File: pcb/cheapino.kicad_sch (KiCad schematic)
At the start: 3 parts

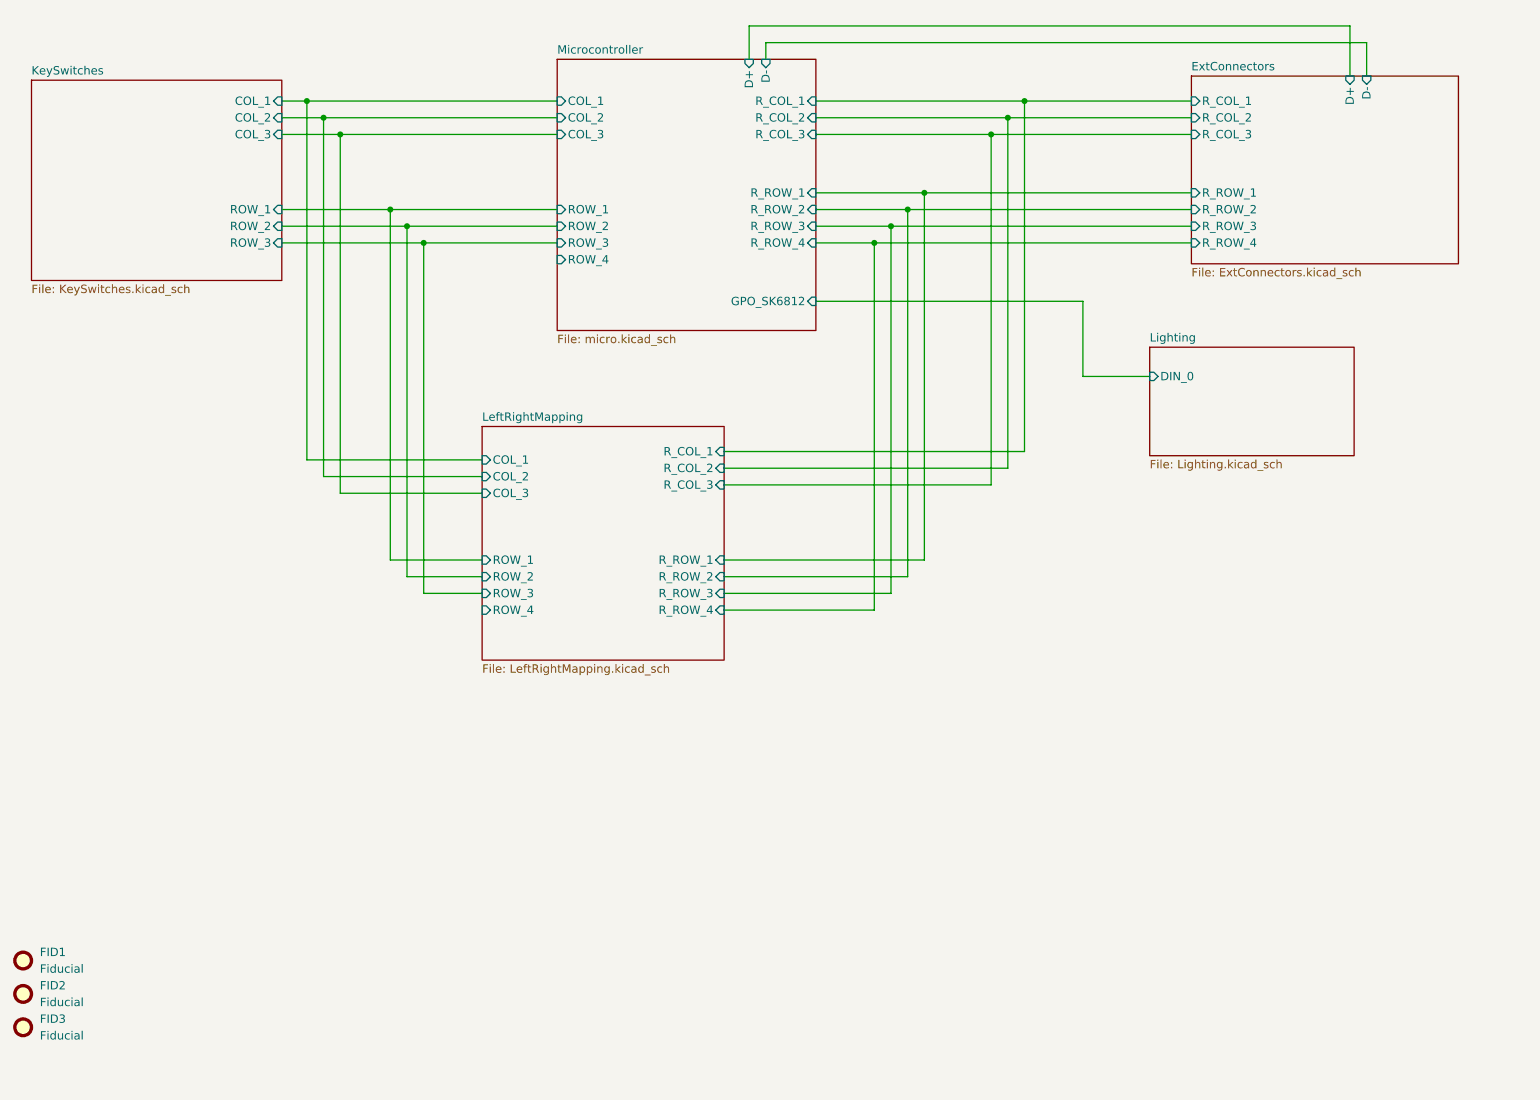
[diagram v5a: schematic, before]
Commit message: Placing more components onto the PCB and removing more stale leftovers from the now absent Rotary Encoder.
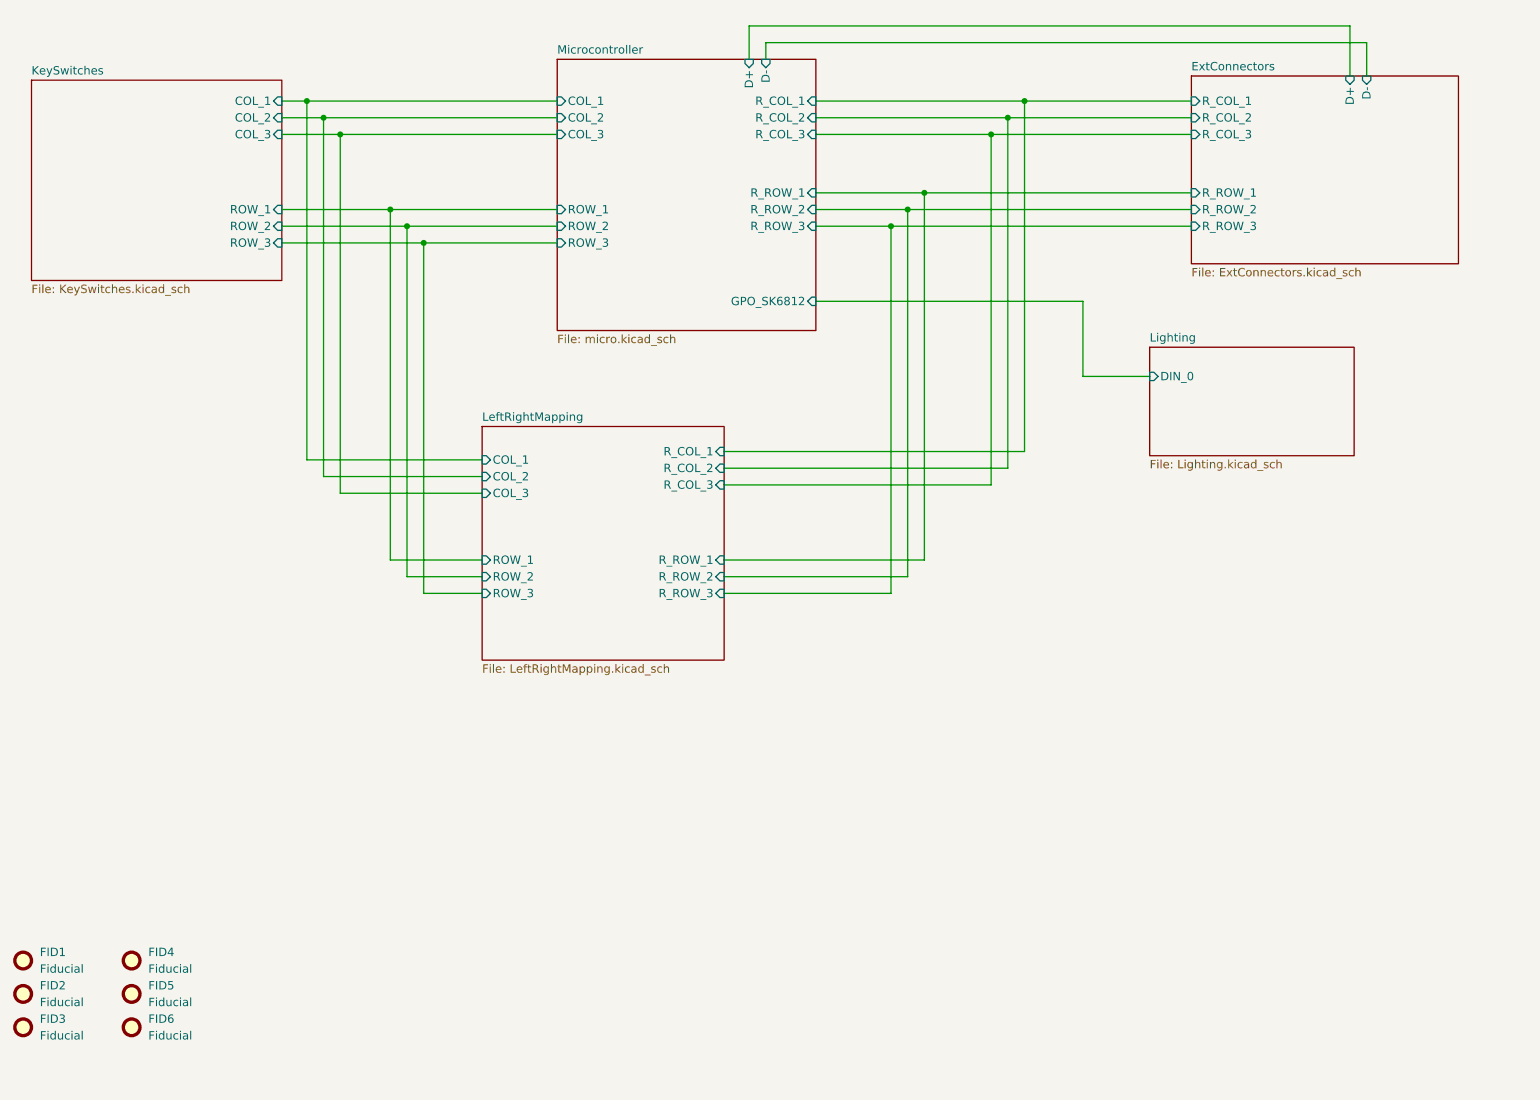
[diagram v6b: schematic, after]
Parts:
- added FID4, FID5, FID6: Fiducial, Fiducial:Fiducial_1mm_Mask2mm, symbol Mechanical:Fiducial
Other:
- sheet ExtConnectors ports: added none; removed R_ROW_4
- sheet LeftRightMapping ports: added none; removed ROW_4, R_ROW_4
- sheet Microcontroller ports: added none; removed ROW_4, R_ROW_4
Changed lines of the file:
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@@
-	)
-	(junction
-		(at 161.29 66.04)
-		(diameter 0)
-		(color 0 0 0 0)
 	)
 	(junction
@@
 	(wire
 		(pts
-			(xy 138.43 121.92) (xy 161.29 121.92)
-		)
-		(stroke
-			(width 0)
-			(type default)
-		)
-	)
-	(wire
-		(pts
 			(xy 166.37 116.84) (xy 138.43 116.84)
 		)
@@
 	(wire
 		(pts
-			(xy 161.29 66.04) (xy 161.29 121.92)
-		)
-		(stroke
-			(width 0)
-			(type default)
-		)
-	)
-	(wire
-		(pts
 			(xy 166.37 60.96) (xy 209.55 60.96)
 		)
@@
 	(wire
 		(pts
-			(xy 161.29 66.04) (xy 152.4 66.04)
-		)
-		(stroke
-			(width 0)
-			(type default)
-		)
-	)
-	(wire
-		(pts
-			(xy 209.55 66.04) (xy 161.29 66.04)
-		)
-		(stroke
-			(width 0)
-			(type default)
-		)
-	)
-	(wire
-		(pts
 			(xy 87.63 60.96) (xy 87.63 114.3)
 		)
@@
 			(width 0)
 			(type default)
+		)
+	)
+	(symbol
+		(lib_id "Mechanical:Fiducial")
+		(at 48.26 185.42 0)
+		(unit 1)
+		(exclude_from_sim yes)
+		(in_bom no)
+		(on_board yes)
+		(dnp no)
+		(fields_autoplaced yes)
+		(property "Reference" "FID6"
+			(at 50.8 184.1499 0)
+			(effects
+				(font
+					(size 1.27 1.27)
+				)
+				(justify left)
+			)
+		)
+		(property "Value" "Fiducial"
+			(at 50.8 186.6899 0)
+			(effects
+				(font
+					(size 1.27 1.27)
+				)
+				(justify left)
+			)
+		)
+		(property "Footprint" "Fiducial:Fiducial_1mm_Mask2mm"
+			(at 48.26 185.42 0)
+			(effects
+				(font
+					(size 1.27 1.27)
+				)
+				(hide yes)
+			)
+		)
+		(property "Datasheet" "~"
+			(at 48.26 185.42 0)
+			(effects
+				(font
+					(size 1.27 1.27)
+				)
+				(hide yes)
+			)
+		)
+		(property "Description" "Fiducial Marker"
+			(at 48.26 185.42 0)
+			(effects
+				(font
+					(size 1.27 1.27)
+				)
+				(hide yes)
+			)
+		)
+		(instances
+			(project "cheapino"
+				(path "/9203b006-47ac-4f34-8cc4-2b709e3df56f"
+					(reference "FID6")
+					(unit 1)
+				)
+			)
+		)
+	)
+	(symbol
+		(lib_id "Mechanical:Fiducial")
+		(at 48.26 180.34 0)
+		(unit 1)
+		(exclude_from_sim yes)
+		(in_bom no)
+		(on_board yes)
+		(dnp no)
+		(fields_autoplaced yes)
+		(property "Reference" "FID5"
+			(at 50.8 179.0699 0)
+			(effects
+				(font
+					(size 1.27 1.27)
+				)
+				(justify left)
+			)
+		)
+		(property "Value" "Fiducial"
+			(at 50.8 181.6099 0)
+			(effects
+				(font
+					(size 1.27 1.27)
+				)
+				(justify left)
+			)
+		)
+		(property "Footprint" "Fiducial:Fiducial_1mm_Mask2mm"
+			(at 48.26 180.34 0)
+			(effects
+				(font
+					(size 1.27 1.27)
+				)
+				(hide yes)
+			)
+		)
+		(property "Datasheet" "~"
+			(at 48.26 180.34 0)
+			(effects
+				(font
+					(size 1.27 1.27)
+				)
+				(hide yes)
+			)
+		)
+		(property "Description" "Fiducial Marker"
+			(at 48.26 180.34 0)
+			(effects
+				(font
+					(size 1.27 1.27)
+				)
+				(hide yes)
+			)
+		)
+		(instances
+			(project "cheapino"
+				(path "/9203b006-47ac-4f34-8cc4-2b709e3df56f"
+					(reference "FID5")
+					(unit 1)
+				)
+			)
 		)
 	)
@@
 	(symbol
 		(lib_id "Mechanical:Fiducial")
+		(at 48.26 175.26 0)
+		(unit 1)
+		(exclude_from_sim yes)
+		(in_bom no)
+		(on_board yes)
+		(dnp no)
+		(fields_autoplaced yes)
+		(property "Reference" "FID4"
+			(at 50.8 173.9899 0)
+			(effects
+				(font
+					(size 1.27 1.27)
+				)
+				(justify left)
+			)
+		)
+		(property "Value" "Fiducial"
+			(at 50.8 176.5299 0)
+			(effects
+				(font
+					(size 1.27 1.27)
+				)
+				(justify left)
+			)
+		)
+		(property "Footprint" "Fiducial:Fiducial_1mm_Mask2mm"
+			(at 48.26 175.26 0)
+			(effects
+				(font
+					(size 1.27 1.27)
+				)
+				(hide yes)
+			)
+		)
+		(property "Datasheet" "~"
+			(at 48.26 175.26 0)
+			(effects
+				(font
+					(size 1.27 1.27)
+				)
+				(hide yes)
+			)
+		)
+		(property "Description" "Fiducial Marker"
+			(at 48.26 175.26 0)
+			(effects
+				(font
+					(size 1.27 1.27)
+				)
+				(hide yes)
+			)
+		)
+		(instances
+			(project "cheapino"
+				(path "/9203b006-47ac-4f34-8cc4-2b709e3df56f"
+					(reference "FID4")
+					(unit 1)
+				)
+			)
+		)
+	)
+	(symbol
+		(lib_id "Mechanical:Fiducial")
 		(at 31.75 185.42 0)
 		(unit 1)
@@
 			)
 		)
-		(pin "R_ROW_4" input
-			(at 138.43 121.92 0)
-			(effects
-				(font
-					(size 1.27 1.27)
-				)
-				(justify right)
-			)
-		)
 		(pin "R_COL_1" input
 			(at 138.43 97.79 0)
@@
 		(pin "ROW_3" input
 			(at 101.6 119.38 180)
-			(effects
-				(font
-					(size 1.27 1.27)
-				)
-				(justify left)
-			)
-		)
-		(pin "ROW_4" input
-			(at 101.6 121.92 180)
 			(effects
 				(font
@@
 			)
 		)
-		(pin "R_ROW_4" input
-			(at 152.4 66.04 0)
-			(effects
-				(font
-					(size 1.27 1.27)
-				)
-				(justify right)
-			)
-		)
-		(pin "ROW_4" input
-			(at 113.03 68.58 180)
-			(effects
-				(font
-					(size 1.27 1.27)
-				)
-				(justify left)
-			)
-		)
 		(pin "R_ROW_3" input
 			(at 152.4 63.5 0)
@@
 			(effects
 				(font
-					(size 1.27 1.27)
-				)
-				(justify left)
-			)
-		)
-		(pin "R_ROW_4" input
-			(at 209.55 66.04 180)
-			(effects
-				(font

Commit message: Replacing 6 channel ESD protection with multiple 2 channel ones.
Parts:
- added H1, H2, H3, H4, H5, H6, H7, H8, H9: MountingHole, MountingHole:MountingHole_2.2mm_M2, symbol Mechanical:MountingHole

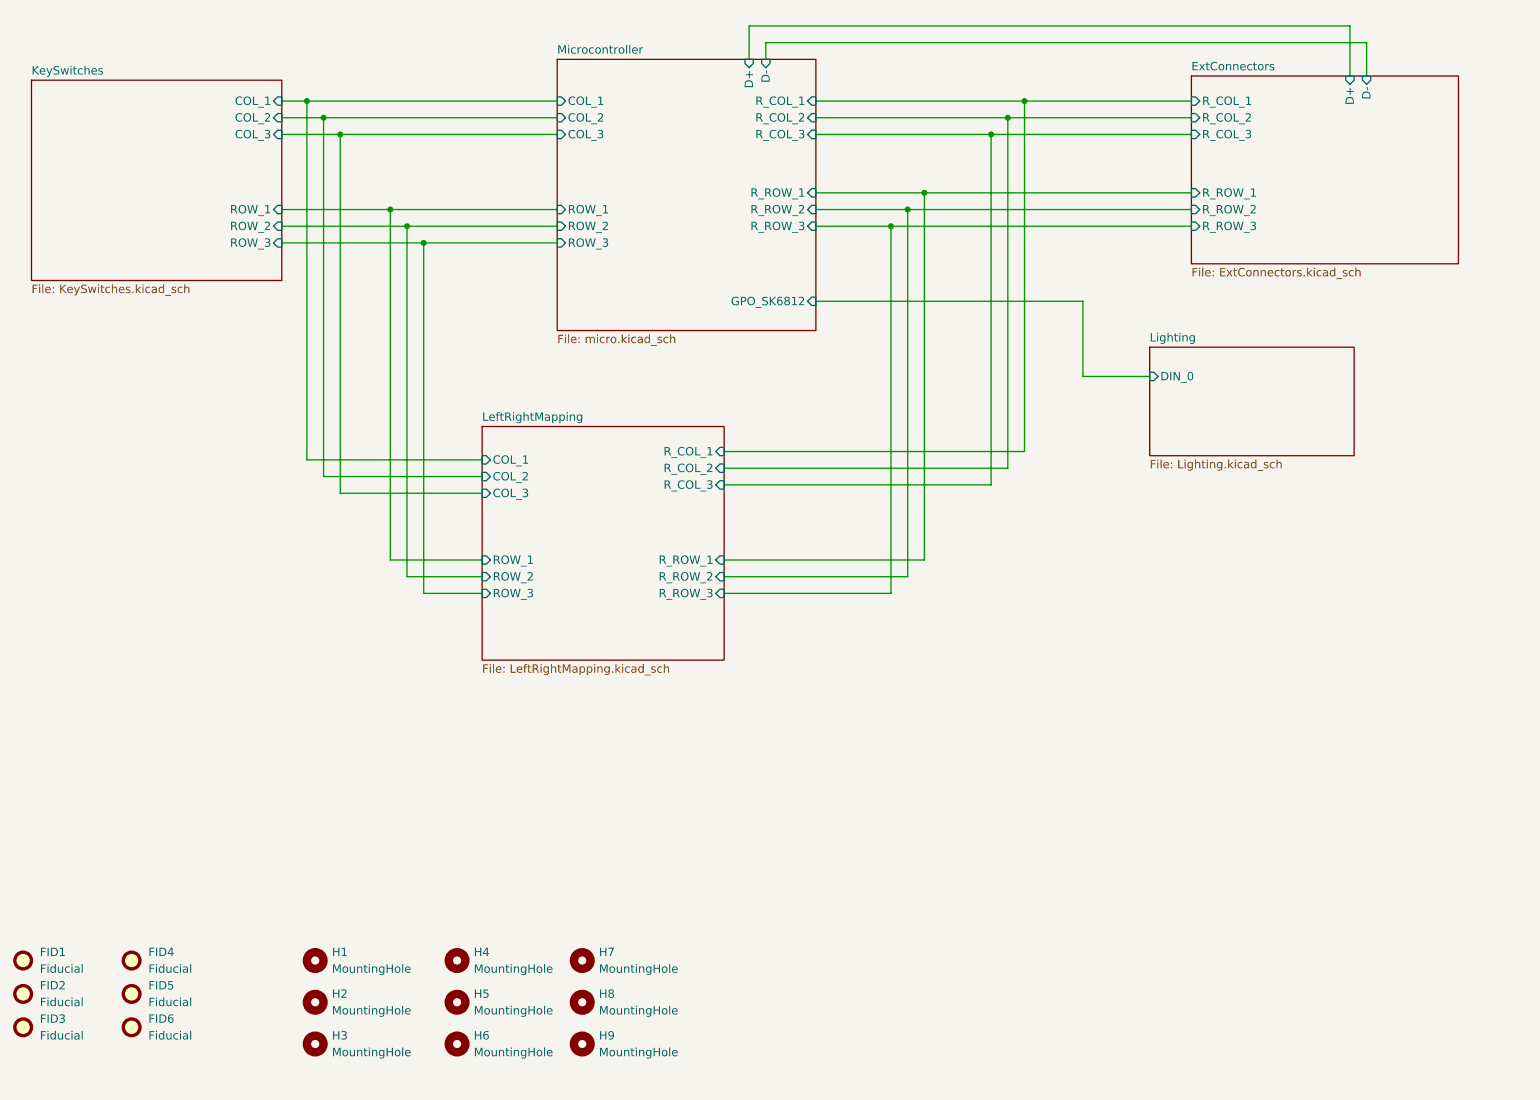
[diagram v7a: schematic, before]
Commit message: WIP: Starting to migrate toward 2 independant halves.
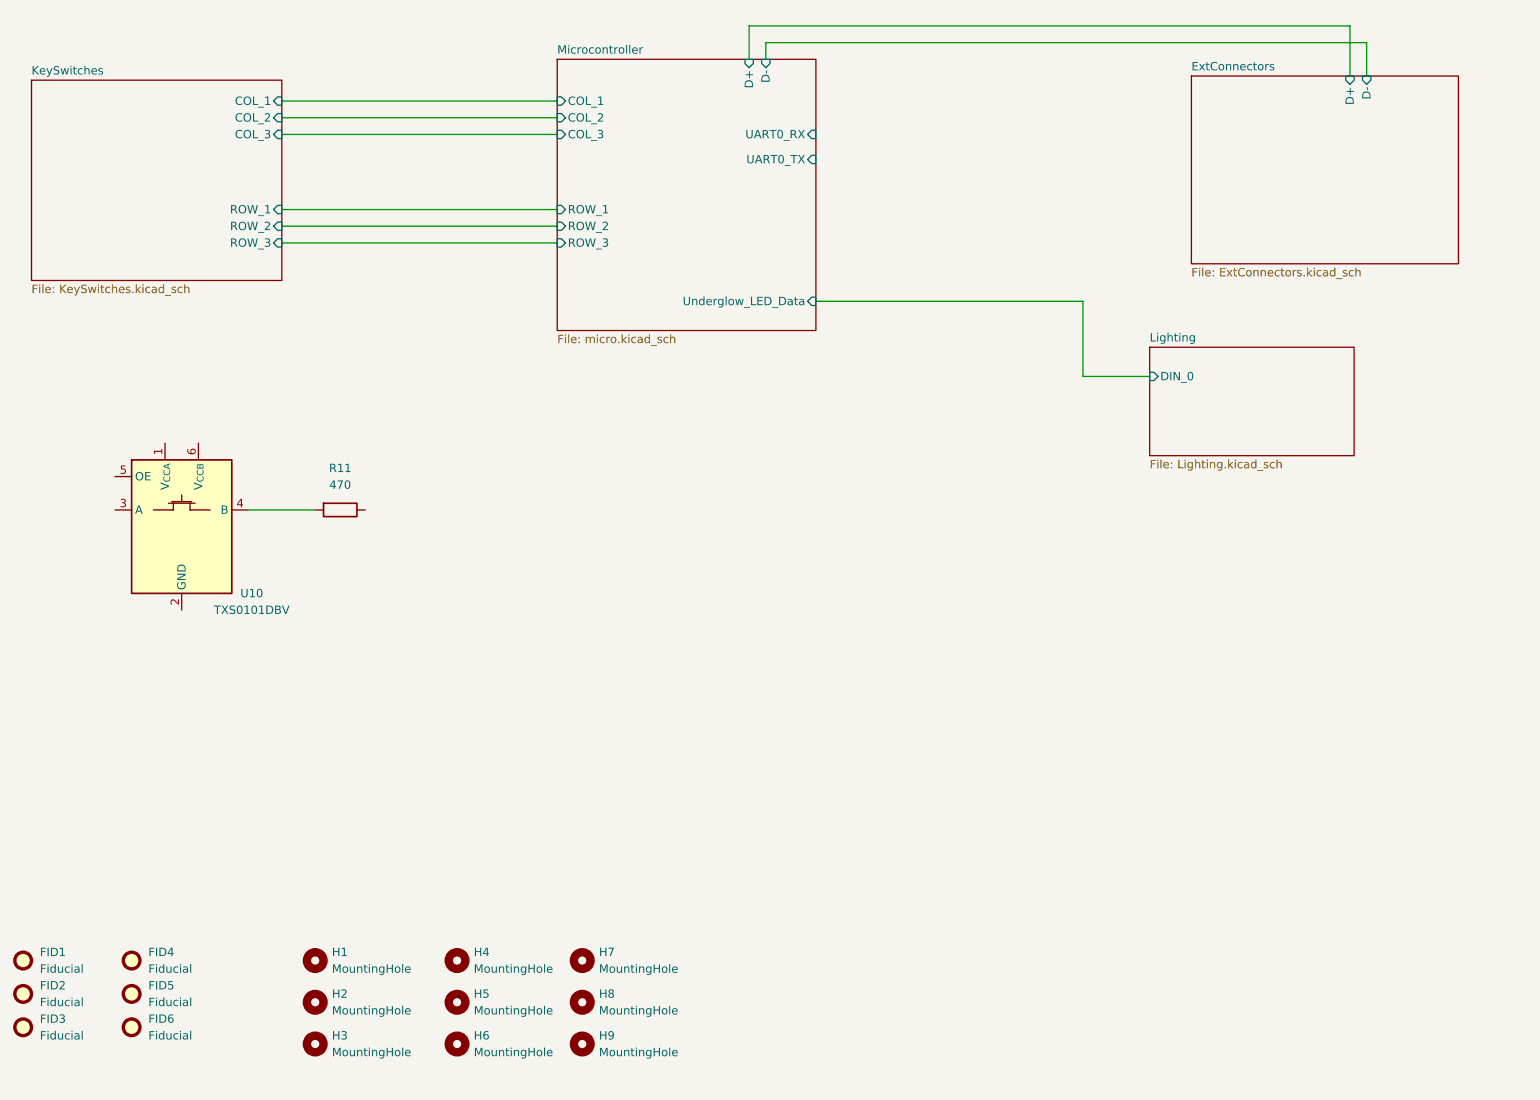
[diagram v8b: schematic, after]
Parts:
- added R11: 470, Resistor_SMD:R_0603_1608Metric_Pad0.98x0.95mm_HandSolder, symbol Device:R
- added U10: TXS0101DBV, Package_TO_SOT_SMD:SOT-23-6, symbol Logic_LevelTranslator:TXS0101DBV
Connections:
- new net: R11.2, U10.4 (B)
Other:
- removed sheet LeftRightMapping
- sheet ExtConnectors ports: added none; removed R_COL_1, R_COL_2, R_COL_3, R_ROW_1, R_ROW_2, R_ROW_3
- sheet Microcontroller ports: added UART0_RX, UART0_TX, Underglow_LED_Data; removed GPO_SK6812, R_COL_1, R_COL_2, R_COL_3, R_ROW_1, R_ROW_2, R_ROW_3
